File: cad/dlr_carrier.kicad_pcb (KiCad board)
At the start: 2 copper layers, 120 x 105 mm, 60 parts, among them J1 PV_IN, J10 YL-83, J11 DEBUG_UART, J2 BQ24650, J3 BAT, J4 LMR33630ADDA, J5 CM4_J2, J6 U.FL, J7 SIM, J8 FLIR_LEPTON, J9 SI1145, U1 AP2112K-3.3, U2 LP5907MFX-3.8, U3 BG770A-NA, U4 TXS0108E, U5 DHT22, U6 ADS1115

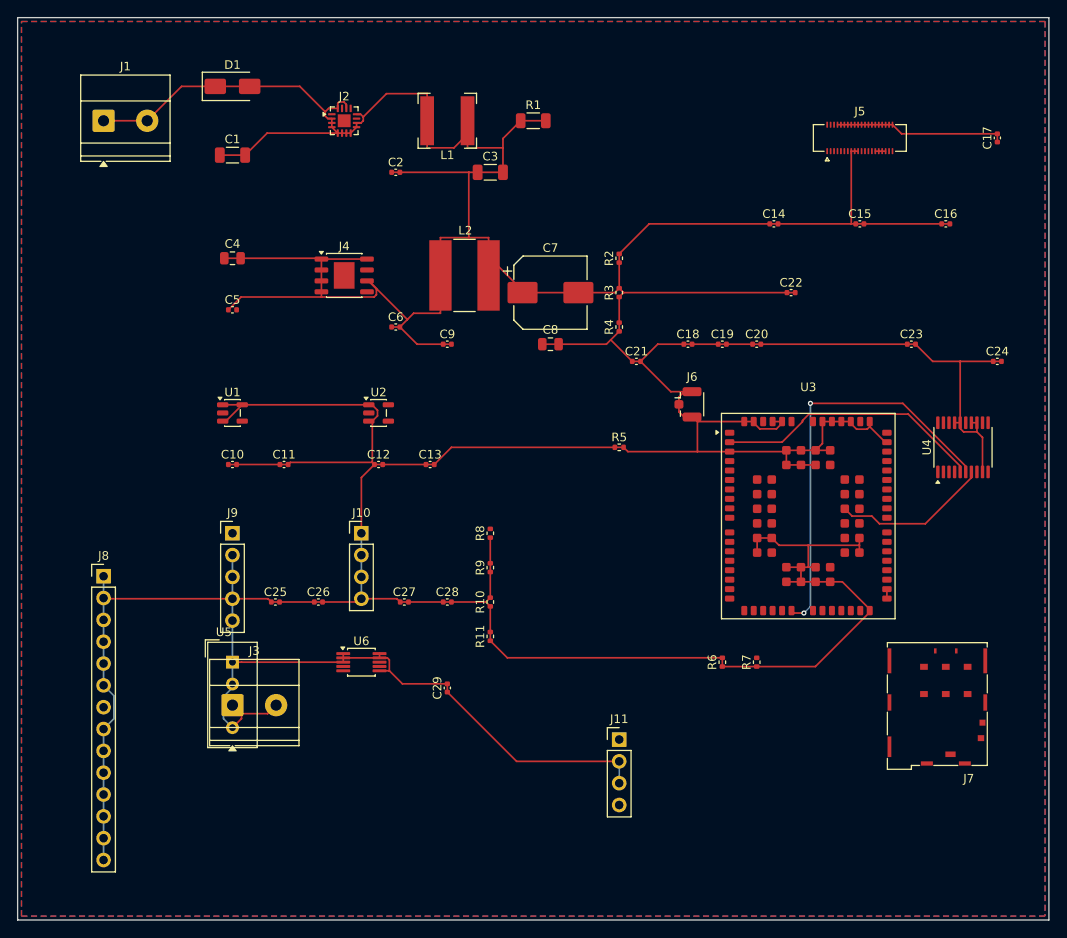
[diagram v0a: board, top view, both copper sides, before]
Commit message: 🗺 feat(cad): scripted schematic + board pipeline, 4-layer stack
The committed board had almost every pad on +3V3 — no 5V_RAIL, VBAT or SDA1 net
existed on it at all — so the gerbers in output/ were never a valid board. Cause:
"Update PCB from Schematic" is GUI-only, so nothing kept the board honest, and the
schematic generator itself was merging nets.

Schematic generator:
  * power stubs now run along the pin direction; they used to be forced up or down
    regardless, which drove a 5V_RAIL stub straight through the buck inductor's
    BUCK_SW pin
  * PWR_FLAGs are placed by rule — any net that reaches a power-input pin with no
    power-output pin gets exactly one — instead of a hardcoded list, which is what
    the new VBAT and CHG_VCC rails needed
  * placement is deterministic; it used Python's salted hash(), so no two runs
    produced the same schematic
  * sch_guard fails the build on any cross-net wire/pin collision
  * ~700 lines of dead single-sheet generator removed
  ERC: 0 violations across all 8 sheets.

Board pipeline (cad/drawing/, all scripted, no GUI step):
  sync_pcb      rebuilds every footprint from the library and reassigns every pad
                net from the SKiDL netlist — the replacement for F8
  board_setup   4-layer SIG/GND/5V/SIG stack, rules, net classes, planes (ADR-016)
  route_pcb     DSN -> Freerouting -> SES, after patching the DSN so plane layers
                are "power" (the router was slicing the planes with signals) and
                the plane declarations are dropped (the router had been leaving
                GND and 5V pads with no path to the plane at all)
  stitch_planes vias from surface pads into their plane
  close_gaps    closes what the router leaves, using real segment-to-segment
                clearance; it never forces copper through another net

DRC: 265 unconnected -> 5, with no clearance, short, annular-ring or courtyard
errors. The remaining 5 are escapes on the DF40, the VQFN and the MSOP; they are
l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
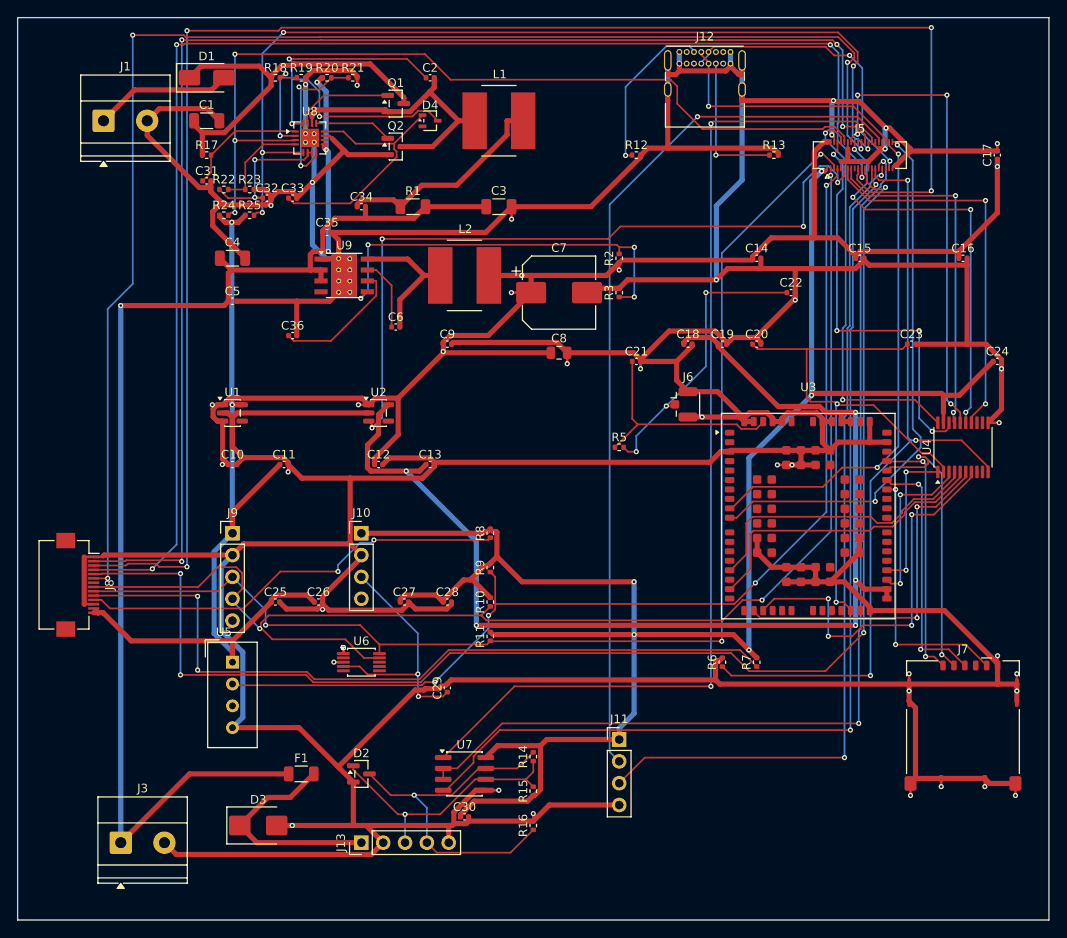
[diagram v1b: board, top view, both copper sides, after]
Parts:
- removed J2: BQ24650, Package_DFN_QFN:HVQFN-16-1EP_3x3mm_P0.5mm_EP1.5x1.5mm
- removed J4: LMR33630ADDA, Package_SO:HSOP-8-1EP_3.9x4.9mm_P1.27mm_EP2.41x3.1mm
- removed R4: 47k, Resistor_SMD:R_0402_1005Metric
- added C30: 100nF, Capacitor_SMD:C_0402_1005Metric, F.Cu at (152.0, 173.0)
- added C31: 1uF, Capacitor_SMD:C_0402_1005Metric, F.Cu at (122.0, 99.0)
- added C32: 1uF, Capacitor_SMD:C_0402_1005Metric, F.Cu at (129.0, 101.0)
- added C33: 1uF, Capacitor_SMD:C_0402_1005Metric, F.Cu at (132.0, 101.0)
- added C34: 100nF, Capacitor_SMD:C_0402_1005Metric, F.Cu at (140.0, 102.0)
- added C35: 100nF, Capacitor_SMD:C_0402_1005Metric, F.Cu at (136.0, 105.0)
- added C36: 1uF, Capacitor_SMD:C_0402_1005Metric, F.Cu at (132.0, 117.0)
- added D2: SM712-like, Package_TO_SOT_SMD:SOT-23, F.Cu at (140.0, 168.0)
- added D3: SMBJ24CA, Diode_SMD:D_SMB, F.Cu at (128.0, 174.0)
- added D4: BAT54W, Package_TO_SOT_SMD:SOT-323_SC-70, F.Cu at (148.0, 92.0)
- added F1: 250mA, Resistor_SMD:R_1206_3216Metric, F.Cu at (133.0, 168.0)
- added J12: USBC_COMMISSIONING, Connector_USB:USB_C_Receptacle_GCT_USB4085, F.Cu at (177.0, 84.0)
- added J13: ANEMO_M12_5P, Connector_PinHeader_2.54mm:PinHeader_1x05_P2.54mm_Vertical, F.Cu at (140.0, 176.0)
- added Q1: DMN4035L-7, Package_TO_SOT_SMD:SOT-23, F.Cu at (144.0, 90.0)
- added Q2: DMN4035L-7, Package_TO_SOT_SMD:SOT-23, F.Cu at (144.0, 95.0)
- added R12: 5.1k, Resistor_SMD:R_0402_1005Metric, F.Cu at (172.0, 96.0)
- added R13: 5.1k, Resistor_SMD:R_0402_1005Metric, F.Cu at (188.0, 96.0)
- added R14: 120, Resistor_SMD:R_0402_1005Metric, F.Cu at (160.0, 166.0)
- added R15: 680, Resistor_SMD:R_0402_1005Metric, F.Cu at (160.0, 170.0)
- added R16: 680, Resistor_SMD:R_0402_1005Metric, F.Cu at (160.0, 174.0)
- added R17: 10, Resistor_SMD:R_0402_1005Metric, F.Cu at (122.0, 96.0)
- added R18: 130k, Resistor_SMD:R_0402_1005Metric, F.Cu at (130.0, 87.0)
- added R19: 10k, Resistor_SMD:R_0402_1005Metric, F.Cu at (133.0, 87.0)
- added R20: 297k, Resistor_SMD:R_0402_1005Metric, F.Cu at (136.0, 87.0)
- added R21: 49.9k, Resistor_SMD:R_0402_1005Metric, F.Cu at (139.0, 87.0)
- added R22: 10k, Resistor_SMD:R_0402_1005Metric, F.Cu at (124.0, 100.0)
- added R23: 15k, Resistor_SMD:R_0402_1005Metric, F.Cu at (127.0, 100.0)
- added R24: 10k, Resistor_SMD:R_0402_1005Metric, F.Cu at (124.0, 103.0)
- added R25: 10k, Resistor_SMD:R_0402_1005Metric, F.Cu at (127.0, 103.0)
- added U7: SP3485EN, Package_SO:SOIC-8_3.9x4.9mm_P1.27mm, F.Cu at (152.0, 168.0)
- added U8: BQ24650RVAR, Package_DFN_QFN:Texas_RVA_VQFN-16-1EP_3.5x3.5mm_P0.5mm_EP2.14x2.14mm_ThermalVias, F.Cu at (134.0, 94.0)
- added U9: LMR33630ADDA, Package_SO:Texas_HSOP-8-1EP_3.9x4.9mm_P1.27mm_ThermalVias, F.Cu at (138.0, 110.0)
- C4: value 4.7uF -> 10uF; footprint Capacitor_SMD:C_0805_2012Metric -> Capacitor_SMD:C_1206_3216Metric
- C5: value 100nF -> 220nF
- J8: value FLIR_LEPTON -> FLIR_LEPTON_FFC; footprint Connector_PinHeader_2.54mm:PinHeader_1x14_P2.54mm_Vertical -> Connector_FFC-FPC:Hirose_FH12-14S-0.5SH_1x14-1MP_P0.50mm_Horizontal
- L1: footprint Inductor_SMD:L_Bourns-SRN6028 -> Inductor_SMD:L_Bourns_SRN8040TA
- L2: footprint Inductor_SMD:L_Bourns-SRN8040_8x8.15mm -> Inductor_SMD:L_Bourns_SRN8040TA
- R2: value 39.2k -> 100k
- R3: value 10k -> 24.9k
- moved J3 20.6 mm to (112.0, 176.0)
- moved R1 17.2 mm to (146.0, 102.0)
- moved C2 11.7 mm to (148.0, 87.0)
- moved L1 6.00 mm to (156.0, 92.0)
- moved C1 5.00 mm to (122.0, 92.0)
- moved C14 4.47 mm to (186.0, 108.0)
- moved C16 4.47 mm to (210.0, 108.0)
- moved J7 4.47 mm to (210.0, 162.0)
- moved C3 4.12 mm to (156.0, 102.0)
- moved C15 4.00 mm to (198.0, 108.0)
- moved D1 3.16 mm to (122.0, 87.0)
- moved J8 3.16 mm to (107.0, 146.0), turned to -90 degrees
- moved C17 2.00 mm to (214.0, 96.0)
- moved J5 2.00 mm to (198.0, 96.0)
- moved C8 1.41 mm to (163.0, 119.0)
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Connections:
- C1 pad 1: +3V3 -> PV_IN
- C1 pad 2: +3V3 -> GND
- C10 pad 1: +3V3 -> 5V_RAIL
- C10 pad 2: +3V3 -> GND
- C11 pad 1: +3V3 -> 3V3
- C11 pad 2: +3V3 -> GND
- C12 pad 1: +3V3 -> 5V_RAIL
- C12 pad 2: +3V3 -> GND
- C13 pad 1: +3V3 -> 3V8_CELL
- C13 pad 2: +3V3 -> GND
- C14 pad 1: +3V3 -> 5V_RAIL
- C14 pad 2: +3V3 -> GND
- C15 pad 1: +3V3 -> 5V_RAIL
- C15 pad 2: +3V3 -> GND
- C16 pad 1: +3V3 -> 5V_RAIL
- C16 pad 2: +3V3 -> GND
- C17 pad 1: +3V3 -> 5V_RAIL
- C17 pad 2: +3V3 -> GND
- C18 pad 1: +3V3 -> 3V8_CELL
- C18 pad 2: +3V3 -> GND
- C19 pad 1: +3V3 -> 3V8_CELL
- C19 pad 2: +3V3 -> GND
- C2 pad 1: +3V3 -> CHG_BTST
- C2 pad 2: +3V3 -> MPPT_SW
- C20 pad 1: +3V3 -> VDD_EXT_1V8
- C20 pad 2: +3V3 -> GND
- C21 pad 1: +3V3 -> ANT_IN
- C21 pad 2: +3V3 -> GND
- C22 pad 1: +3V3 -> ANT_MATCH
- C22 pad 2: +3V3 -> GND
- C23 pad 1: +3V3 -> VDD_EXT_1V8
- C23 pad 2: +3V3 -> GND
- C24 pad 1: +3V3 -> 3V3
- C24 pad 2: +3V3 -> GND
- C25 pad 1: +3V3 -> 3V3
- C25 pad 2: +3V3 -> GND
- C26 pad 1: +3V3 -> 3V3
- C26 pad 2: +3V3 -> GND
- C27 pad 1: +3V3 -> 3V3
- C27 pad 2: +3V3 -> GND
- C28 pad 1: +3V3 -> 3V3
- C28 pad 2: +3V3 -> GND
- C29 pad 1: +3V3 -> RAIN_AO
- C29 pad 2: +3V3 -> GND
- C3 pad 1: +3V3 -> VBAT
- C3 pad 2: +3V3 -> GND
- C4 pad 1: +3V3 -> VBAT
- C4 pad 2: +3V3 -> GND
- C5 pad 1: +3V3 -> VBAT
- C6 pad 1: +3V3 -> BUCK_BOOT
- C6 pad 2: +3V3 -> BUCK_SW
- C7 pad 1: +3V3 -> 5V_RAIL
- C7 pad 2: +3V3 -> GND
- C8 pad 1: +3V3 -> 5V_RAIL
- C8 pad 2: +3V3 -> GND
- C9 pad 1: +3V3 -> 5V_RAIL
- C9 pad 2: +3V3 -> GND
- D1 pad 1: +3V3 -> PV_IN
- D1 pad 2: +3V3 -> PV_RAW
- J1 pad 1: +3V3 -> PV_RAW
- J1 pad 2: +3V3 -> GND
- J10 pad 1: +3V3 -> 3V3
- J10 pad 2: +3V3 -> GND
- J10 pad 3: +3V3 -> RAIN_AO
- J10 pad 4: +3V3 -> unconnected-(J10-Pad4)
- J11 pad 1: /DBG_RX -> 3V3
- J11 pad 2: +3V3 -> DBG_TX
- J11 pad 3: +3V3 -> DBG_RX
- J11 pad 4: unconnected-(J11-Pin_4-Pad4) -> GND
- J3 pad 1: +3V3 -> VBAT
- J3 pad 2: +3V3 -> GND
- J5 pad 1: +3V3 -> 3V3
- J5 pad 10: +3V3 -> UART_RX_3V3
- J5 pad 11: /USB_DP -> CELL_EN
- J5 pad 12: +3V3 -> CHG_STAT1
- J5 pad 13: +3V3 -> CELL_NET_STATUS
- J5 pad 14: +3V3 -> GND
- J5 pad 15: +3V3 -> CELL_PWRKEY
- J5 pad 16: +3V3 -> CELL_RESET
- J5 pad 17: +3V3 -> 3V3
- J5 pad 18: +3V3 -> CELL_STATUS
- J5 pad 19: +3V3 -> SPI0_MOSI
- J5 pad 2: unconnected-(J5-Pin_2-Pad2) -> 5V_RAIL
- J5 pad 20: +3V3 -> GND
- J5 pad 21: +3V3 -> SPI0_MISO
- J5 pad 22: +3V3 -> GPIO25_VSYNC
- J5 pad 23: /CELL_PWRKEY -> SPI0_SCLK
- J5 pad 24: +3V3 -> SPI0_CE0
- J5 pad 25: /CELL_NET_STATUS -> GND
- J5 pad 26: +3V3 -> CHG_STAT2
- J5 pad 27: +3V3 -> ANEMO_UART_TX
- J5 pad 28: +3V3 -> ANEMO_UART_RX
- J5 pad 29: +3V3 -> SHIFTER_OE
- J5 pad 3: +3V3 -> SDA1
- J5 pad 30: +3V3 -> GND
- J5 pad 31: +3V3 -> ANEMO_DE
- J5 pad 32: +3V3 -> DBG_TX
- J5 pad 33: +3V3 -> DBG_RX
- J5 pad 34: +3V3 -> GND
- J5 pad 35: +3V3 -> unconnected-(J5-Pad35)
- J5 pad 36: +3V3 -> USB_CMSN_DP
- J5 pad 37: +3V3 -> USB_CMSN_DM
- J5 pad 38: +3V3 -> USB_DP
- J5 pad 39: unconnected-(J5-Pin_39-Pad39) -> GND
- J5 pad 4: unconnected-(J5-Pin_4-Pad4) -> 5V_RAIL
- J5 pad 40: +3V3 -> USB_DM
- J5 pad 5: /DBG_RX -> SCL1
- J5 pad 6: +3V3 -> GND
- J5 pad 7: unconnected-(J5-Pin_7-Pad7) -> GPIO4_DHT22
- J5 pad 8: +3V3 -> UART_TX_3V3
- J5 pad 9: +3V3 -> GND
- J6 pad 1: +3V3 -> ANT_MATCH
- J6 pad 2: +3V3 -> GND
- J7 pad SH: (no net) -> GND
- J8 pad 1: +3V3 -> GND
- J8 pad 10: +3V3 -> N$5
- J8 pad 11: +3V3 -> N$6
- J8 pad 12: +3V3 -> GND
- J8 pad 13: +3V3 -> 3V3
- J8 pad 14: +3V3 -> 3V3
- J8 pad 2: +3V3 -> SPI0_CE0
- J8 pad 3: +3V3 -> SPI0_MOSI
- J8 pad 4: +3V3 -> SPI0_MISO
- J8 pad 5: +3V3 -> SPI0_SCLK
- J8 pad 6: +3V3 -> GPIO25_VSYNC
- J8 pad 8: +3V3 -> SDA1
- J8 pad 9: +3V3 -> SCL1
- J9 pad 1: unconnected-(J9-Pin_1-Pad1) -> 3V3
- J9 pad 2: +3V3 -> GND
- J9 pad 3: +3V3 -> SCL1
- J9 pad 4: +3V3 -> SDA1
- J9 pad 5: +3V3 -> unconnected-(J9-Pad5)
- L1 pad 1: +3V3 -> MPPT_SW
- L1 pad 2: +3V3 -> BAT_SRP
- L2 pad 1: +3V3 -> BUCK_SW
- L2 pad 2: +3V3 -> 5V_RAIL
- R1 pad 1: +3V3 -> BAT_SRP
- R1 pad 2: +3V3 -> VBAT
- R10 pad 1: +3V3 -> SDA1
- R10 pad 2: +3V3 -> 3V3
- R11 pad 1: +3V3 -> SCL1
- R11 pad 2: +3V3 -> 3V3
- R2 pad 1: +3V3 -> 5V_RAIL
- R2 pad 2: +3V3 -> BUCK_FB
- R3 pad 1: +3V3 -> BUCK_FB
- R3 pad 2: +3V3 -> GND
- R5 pad 1: +3V3 -> ANT_IN
- R5 pad 2: +3V3 -> ANT_MATCH
- R6 pad 1: +3V3 -> SHIFTER_OE
- R6 pad 2: +3V3 -> GND
- R7 pad 1: +3V3 -> N$5
- R7 pad 2: unconnected-(R7-Pad2) -> 3V3
- R8 pad 1: +3V3 -> N$6
- R8 pad 2: unconnected-(R8-Pad2) -> 3V3
- R9 pad 1: +3V3 -> GPIO4_DHT22
- R9 pad 2: +3V3 -> 3V3
- U1 pad 1: +3V3 -> 5V_RAIL
- U1 pad 2: unconnected-(U1-GND-Pad2) -> GND
- U1 pad 3: +3V3 -> 5V_RAIL
- U1 pad 5: +3V3 -> 3V3
- U2 pad 1: +3V3 -> 5V_RAIL
- U2 pad 2: unconnected-(U2-GND-Pad2) -> GND
- U2 pad 3: +3V3 -> CELL_EN
- U2 pad 5: unconnected-(U2-OUT-Pad5) -> 3V8_CELL
- U3 pad 1: unconnected-(U3-PSM_IND-Pad1) -> (no net)
- U3 pad 10: unconnected-(U3-USB_DM-Pad10) -> USB_DM
- U3 pad 100: +3V3 -> GND
- U3 pad 101: +3V3 -> GND
- U3 pad 102: +3V3 -> GND
- U3 pad 11: unconnected-(U3-RESERVED-Pad11) -> (no net)
- U3 pad 12: unconnected-(U3-RESERVED-Pad12) -> (no net)
- U3 pad 13: unconnected-(U3-RESERVED-Pad13) -> (no net)
- U3 pad 14: unconnected-(U3-RESERVED-Pad14) -> (no net)
- U3 pad 15: unconnected-(U3-PWRKEY-Pad15) -> CELL_PWRKEY_1V8
- U3 pad 16: unconnected-(U3-RESERVED-Pad16) -> (no net)
- U3 pad 17: unconnected-(U3-~{RESET}-Pad17) -> CELL_RESET_1V8
- U3 pad 18: unconnected-(U3-GPIO5-Pad18) -> (no net)
- U3 pad 19: unconnected-(U3-GPIO6-Pad19) -> (no net)
- U3 pad 2: /CELL_RESET_1V8 -> (no net)
- U3 pad 20: unconnected-(U3-STATUS-Pad20) -> CELL_STATUS_1V8
- U3 pad 21: unconnected-(U3-NET_STATUS-Pad21) -> CELL_NET_1V8
- U3 pad 22: unconnected-(U3-GPIO7-Pad22) -> (no net)
- U3 pad 23: unconnected-(U3-GPIO8-Pad23) -> (no net)
- U3 pad 24: /CELL_PWRKEY_1V8 -> (no net)
- U3 pad 25: unconnected-(U3-GPIO9-Pad25) -> (no net)
- U3 pad 26: unconnected-(U3-GPIO10-Pad26) -> (no net)
- U3 pad 27: unconnected-(U3-GPIO11-Pad27) -> (no net)
- U3 pad 28: unconnected-(U3-GPIO12-Pad28) -> (no net)
- U3 pad 29: unconnected-(U3-VDD_EXT-Pad29) -> VDD_EXT_1V8
- U3 pad 3: +3V3 -> GND
- U3 pad 30: unconnected-(U3-MAIN_DTR-Pad30) -> (no net)
- U3 pad 31: +3V3 -> GND
- U3 pad 32: Net-(U3-VBAT_BB-Pad32) -> 3V8_CELL
- U3 pad 33: Net-(U3-VBAT_BB-Pad32) -> 3V8_CELL
- U3 pad 34: unconnected-(U3-MAIN_RXD-Pad34) -> CELL_RX_1V8
- U3 pad 35: unconnected-(U3-MAIN_TXD-Pad35) -> CELL_TX_1V8
- U3 pad 36: unconnected-(U3-MAIN_CTS-Pad36) -> (no net)
- U3 pad 37: unconnected-(U3-MAIN_RTS-Pad37) -> (no net)
- U3 pad 38: unconnected-(U3-MAIN_DCD-Pad38) -> (no net)
- U3 pad 39: unconnected-(U3-MAIN_RI-Pad39) -> (no net)
- U3 pad 4: unconnected-(U3-GPIO1-Pad4) -> (no net)
- U3 pad 40: unconnected-(U3-GPIO13-Pad40) -> (no net)
- U3 pad 41: unconnected-(U3-GPIO14-Pad41) -> (no net)
- U3 pad 42: unconnected-(U3-USIM_DET-Pad42) -> (no net)
- U3 pad 43: unconnected-(U3-USIM_VDD-Pad43) -> N$1
- U3 pad 44: unconnected-(U3-USIM_RST-Pad44) -> N$2
- U3 pad 45: unconnected-(U3-USIM_DATA-Pad45) -> N$4
- U3 pad 46: unconnected-(U3-USIM_CLK-Pad46) -> N$3
- U3 pad 47: unconnected-(U3-USIM_GND-Pad47) -> (no net)
- U3 pad 48: +3V3 -> GND
- U3 pad 49: unconnected-(U3-ANT_GNSS-Pad49) -> (no net)
- U3 pad 5: unconnected-(U3-GPIO2-Pad5) -> (no net)
- U3 pad 50: +3V3 -> GND
- U3 pad 51: unconnected-(U3-RESERVED-Pad51) -> (no net)
- U3 pad 52: +3V3 -> 3V8_CELL
- U3 pad 53: +3V3 -> 3V8_CELL
- U3 pad 54: +3V3 -> GND
- U3 pad 55: +3V3 -> GND
- U3 pad 56: unconnected-(U3-ANT_WIFI-Pad56) -> (no net)
- U3 pad 57: unconnected-(U3-RESERVED-Pad57) -> (no net)
- U3 pad 58: +3V3 -> GND
- U3 pad 59: +3V3 -> GND
- U3 pad 6: unconnected-(U3-GPIO3-Pad6) -> (no net)
- U3 pad 60: unconnected-(U3-ANT_MAIN-Pad60) -> ANT_IN
- U3 pad 61: +3V3 -> GND
- U3 pad 62: +3V3 -> GND
- U3 pad 63: unconnected-(U3-RESERVED-Pad63) -> (no net)
- U3 pad 64: unconnected-(U3-GPIO15-Pad64) -> (no net)
- U3 pad 65: unconnected-(U3-GPIO16-Pad65) -> (no net)
- U3 pad 66: unconnected-(U3-GPIO17-Pad66) -> (no net)
- U3 pad 67: +3V3 -> GND
- U3 pad 68: +3V3 -> GND
- U3 pad 69: +3V3 -> GND
- U3 pad 7: unconnected-(U3-GPIO4-Pad7) -> (no net)
- U3 pad 70: +3V3 -> GND
- U3 pad 71: +3V3 -> GND
- U3 pad 72: +3V3 -> GND
- U3 pad 73: +3V3 -> GND
- U3 pad 74: +3V3 -> GND
- U3 pad 75: /CELL_STATUS_1V8 -> (no net)
- U3 pad 76: unconnected-(U3-RESERVED-Pad76) -> (no net)
- U3 pad 77: unconnected-(U3-RESERVED-Pad77) -> (no net)
- U3 pad 78: unconnected-(U3-RESERVED-Pad78) -> (no net)
- U3 pad 79: +3V3 -> GND
- U3 pad 8: unconnected-(U3-VBUS-Pad8) -> (no net)
- U3 pad 80: +3V3 -> GND
- U3 pad 81: +3V3 -> GND
- U3 pad 82: +3V3 -> GND
- U3 pad 83: unconnected-(U3-GRFC1-Pad83) -> (no net)
- U3 pad 84: unconnected-(U3-GRFC2-Pad84) -> (no net)
- U3 pad 85: unconnected-(U3-GPIO18-Pad85) -> (no net)
- U3 pad 86: unconnected-(U3-GPIO19-Pad86) -> (no net)
- U3 pad 87: +3V3 -> (no net)
- U3 pad 88: unconnected-(U3-GPIO21-Pad88) -> (no net)
- U3 pad 89: +3V3 -> GND
- U3 pad 9: unconnected-(U3-USB_DP-Pad9) -> USB_DP
- U3 pad 90: +3V3 -> GND
- U3 pad 91: +3V3 -> GND
- U3 pad 92: unconnected-(U3-RESERVED-Pad92) -> (no net)
- U3 pad 93: unconnected-(U3-RESERVED-Pad93) -> (no net)
- U3 pad 94: unconnected-(U3-RESERVED-Pad94) -> (no net)
- U3 pad 95: unconnected-(U3-RESERVED-Pad95) -> (no net)
- U3 pad 96: /CELL_RX_1V8 -> (no net)
- U3 pad 97: unconnected-(U3-RESERVED-Pad97) -> (no net)
- U3 pad 98: unconnected-(U3-RESERVED-Pad98) -> (no net)
- U3 pad 99: unconnected-(U3-RESERVED-Pad99) -> (no net)
- U4 pad 1: unconnected-(U4-A1-Pad1) -> CELL_TX_1V8
- U4 pad 10: unconnected-(U4-OE-Pad10) -> SHIFTER_OE
- U4 pad 11: unconnected-(U4-GND-Pad11) -> GND
- U4 pad 13: +3V3 -> unconnected-(U4-Pad13)
- U4 pad 14: +3V3 -> CELL_NET_STATUS
- U4 pad 15: /CELL_PWRKEY -> CELL_STATUS
- U4 pad 16: +3V3 -> CELL_RESET
- U4 pad 17: +3V3 -> CELL_PWRKEY
- U4 pad 18: /CELL_NET_STATUS -> UART_TX_3V3
- U4 pad 19: unconnected-(U4-VCCB-Pad19) -> 3V3
- U4 pad 2: unconnected-(U4-VCCA-Pad2) -> VDD_EXT_1V8
- U4 pad 20: unconnected-(U4-B1-Pad20) -> UART_RX_3V3
- U4 pad 3: /CELL_NET_1V8 -> CELL_RX_1V8
- U4 pad 4: /CELL_STATUS_1V8 -> CELL_PWRKEY_1V8
- U4 pad 5: /CELL_RESET_1V8 -> CELL_RESET_1V8
- U4 pad 6: /CELL_PWRKEY_1V8 -> CELL_STATUS_1V8
- U4 pad 7: /CELL_RX_1V8 -> CELL_NET_1V8
- U4 pad 8: /CELL_TX_1V8 -> unconnected-(U4-Pad8)
- U4 pad 9: +3V3 -> unconnected-(U4-Pad9)
- U5 pad 1: +3V3 -> 3V3
- U5 pad 2: +3V3 -> GPIO4_DHT22
- U5 pad 3: unconnected-(U5-NC-Pad3) -> (no net)
- U5 pad 4: +3V3 -> GND
- U6 pad 1: +3V3 -> GND
- U6 pad 10: +3V3 -> SCL1
- U6 pad 2: +3V3 -> unconnected-(U6-Pad2)
- U6 pad 3: +3V3 -> GND
- U6 pad 4: unconnected-(U6-AIN0-Pad4) -> RAIN_AO
- U6 pad 6: +3V3 -> unconnected-(U6-Pad6)
- U6 pad 8: unconnected-(U6-VDD-Pad8) -> 3V3
- U6 pad 9: +3V3 -> SDA1
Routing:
- net GND: track 0.00 -> 974.5 mm, vias 0 -> 38
- net +3V3: track 806.4 -> 0.00 mm
- net 3V3: track 0.00 -> 324.4 mm, vias 0 -> 7
- net SPI0_MOSI: track 0.00 -> 189.9 mm, vias 0 -> 4
- net 5V_RAIL: track 0.00 -> 170.7 mm, vias 0 -> 8
- net VBAT: track 0.00 -> 165.2 mm, vias 0 -> 4
- net GPIO25_VSYNC: track 0.00 -> 164.0 mm, vias 0 -> 4
- net SPI0_MISO: track 0.00 -> 163.3 mm, vias 0 -> 4
- net SPI0_SCLK: track 0.00 -> 163.1 mm, vias 0 -> 4
- net SPI0_CE0: track 0.00 -> 161.2 mm, vias 0 -> 4
- net SDA1: track 0.00 -> 157.7 mm, vias 0 -> 3
- net SCL1: track 0.00 -> 143.2 mm, vias 0 -> 3
- net 3V8_CELL: track 0.00 -> 137.4 mm, vias 0 -> 5
- net GPIO4_DHT22: track 0.00 -> 123.4 mm, vias 0 -> 4
- net ANEMO_UART_RX: track 0.00 -> 120.2 mm, vias 0 -> 2
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- added copper zone on In2.Cu, net 5V_RAIL
- added copper zone on In1.Cu, net GND
- removed copper zone on F.Cu, net +3V3
- removed copper zone on B.Cu, net GND
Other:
- copper layers 2 -> 4

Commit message: 🩺 fix(pcb): close three fine-pitch escapes and the duplicate drill hits
The escape router and the rip-up loop take the board from 5 open connections to
2: U6.8 (MSOP-10 3V3), U8.10 (VQFN BAT_SRP) and J5.17 (DF40 3V3) are routed, and
the plane-net trunks that ran through the DF40 fanout band are gone — GND now
drops into In1.Cu where those trunks used to fence the pad rows in.

Five vias that shared a hole, and two more whose 0.3 mm drills sat 0.03 mm apart
and would have broken into each other, are removed. DRC is now clean of
clearance, short, annular-ring, hole and courtyard errors; 7 silkscreen-overlap
warnings and the 2 open pins are all that is left.

Both open pins are DF40 grounds (J5.20, J5.25) and both are a fanout-capacity
limit rather than a search failure: a row of 0.6 mm escape vias needs 0.75 mm
centre to centre, so a 0.4 mm pad pitch fits a via on every other pin, and the
0.15 mm slot between two adjacent vias cannot pass the trace that a second,
deeper row would need. Rows have to be assigned before routing; a greedy per-pin
router finishes one slot short. ADR-018 and the readme carry the analysis and
the three ways to close it.

Co-Authored-By: Claude Opus 5 <noreply@anthropic.com>
Claude-Session: https://claude.ai/code/session_011xr7VCL7rkJj2WE2uQF7sF
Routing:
- net 3V3: track 324.4 -> 410.0 mm, vias 7 -> 12
- net BAT_SRP: track 25.2 -> 34.1 mm, vias 0 -> 2
- net GND: track 974.5 -> 975.2 mm, vias 38 -> 37
- net SDA1: track 157.7 -> 158.3 mm
